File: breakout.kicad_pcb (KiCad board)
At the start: 2 copper layers, 24.1 x 52.9 mm, 5 parts

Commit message: Removed right edges fromt races.
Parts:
- added REF**: Vishay_PowerPAK_SC70-6L_Single, Package_TO_SOT_SMD:Vishay_PowerPAK_SC70-6L_Single, F.Cu at (124.7, 90.7)
- added REF**: Vishay_PowerPAK_SC70-6L_Dual, Package_TO_SOT_SMD:Vishay_PowerPAK_SC70-6L_Dual, F.Cu at (119.4, 104.4)
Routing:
- net (no net): track 946.0 -> 938.4 mm

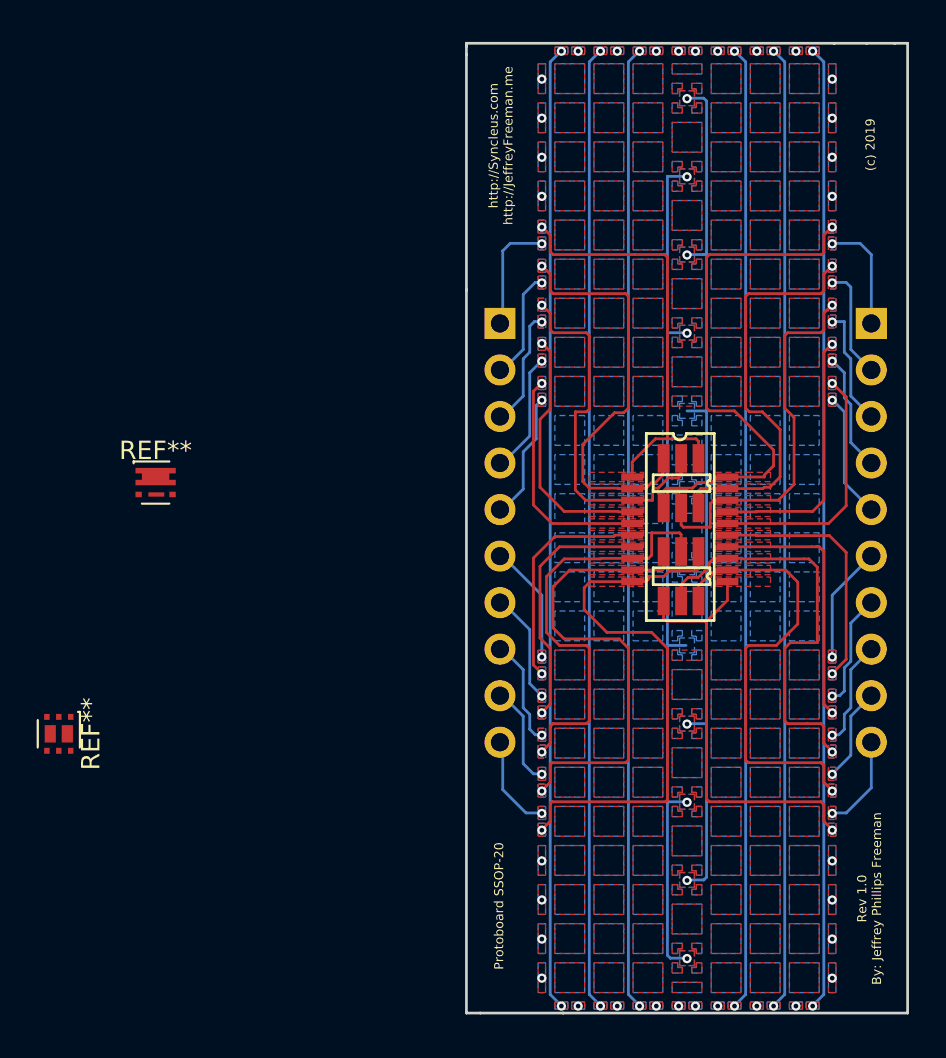
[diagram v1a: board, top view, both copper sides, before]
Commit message: Added labels for pin numbers and a few otehr graphics ont he silk screen.
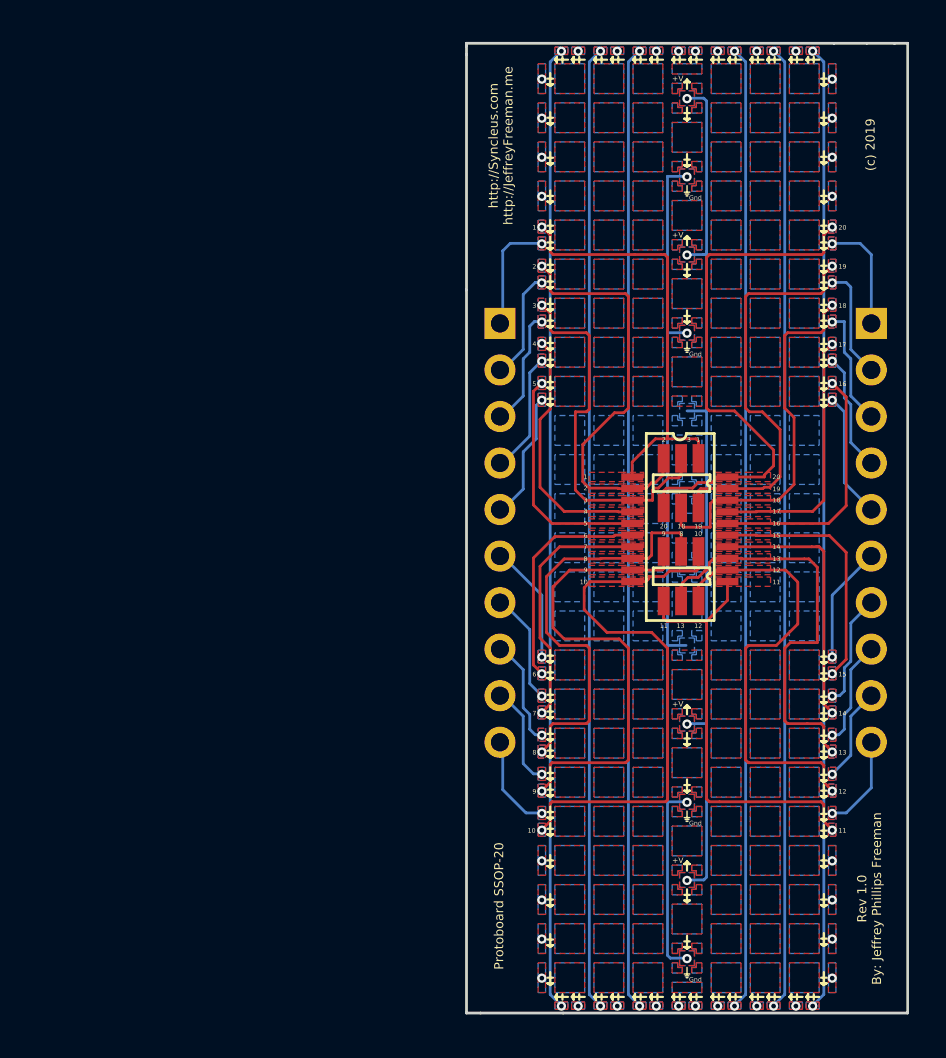
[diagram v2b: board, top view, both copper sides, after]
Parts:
- removed REF**: Vishay_PowerPAK_SC70-6L_Single, Package_TO_SOT_SMD:Vishay_PowerPAK_SC70-6L_Single
- removed REF**: Vishay_PowerPAK_SC70-6L_Dual, Package_TO_SOT_SMD:Vishay_PowerPAK_SC70-6L_Dual
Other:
- board text added: "+V"
- board text added: "1"
- board text added: "10"
- board text added: "11"
- board text added: "12"
- board text added: "13"
- board text added: "14"
- board text added: "15"
- board text added: "16"
- board text added: "17"
- board text added: "18"
- board text added: "19"
- board text added: "2"
- board text added: "20"
- board text added: "3"
- board text added: "4"
- board text added: "5"
- board text added: "6"
- board text added: "7"
- board text added: "8"
- board text added: "9"
- board text added: "Gnd"

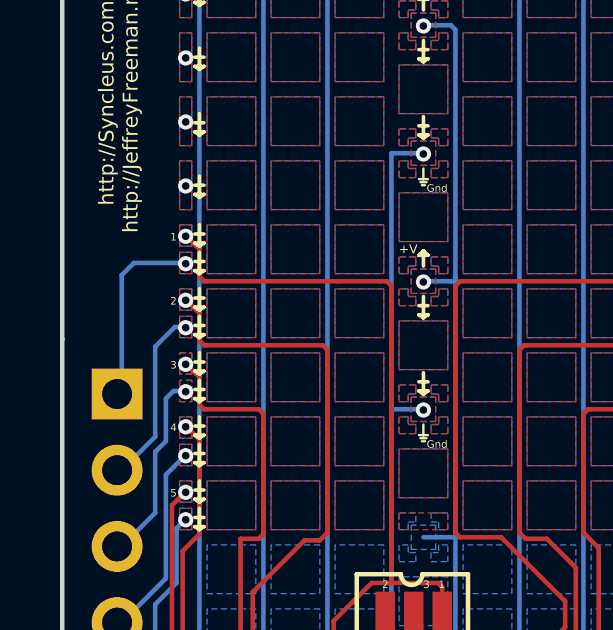
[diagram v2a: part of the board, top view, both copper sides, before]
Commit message: Changed fotn size a bit.
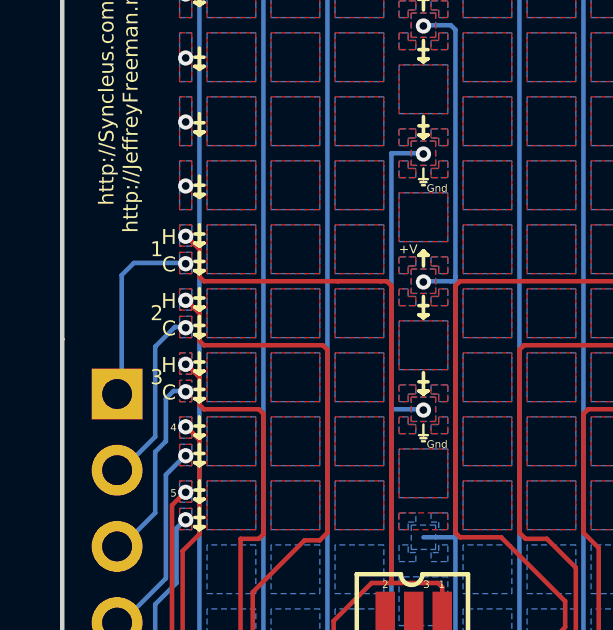
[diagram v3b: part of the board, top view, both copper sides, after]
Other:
- board text added: "C"
- board text added: "H"
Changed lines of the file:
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@@
   (general
     (thickness 1.6)
-    (drawings 1141)
+    (drawings 1147)
     (tracks 527)
     (zones 0)
@@
       (rotate (xyz 0 0 0))
     )
+  )
+  (gr_text 3 (at 144.8308 81.4832) (layer F.SilkS)
+    (effects (font (size 0.5 0.5) (thickness 0.0625)))
+  )
+  (gr_text H (at 145.2372 81.0768) (layer F.SilkS)
+    (effects (font (size 0.5 0.5) (thickness 0.0625)))
+  )
+  (gr_text C (at 145.2372 81.9912) (layer F.SilkS)
+    (effects (font (size 0.5 0.5) (thickness 0.0625)))
+  )
+  (gr_text 2 (at 144.8308 79.3496) (layer F.SilkS)
+    (effects (font (size 0.5 0.5) (thickness 0.0625)))
+  )
+  (gr_text H (at 145.2372 78.9432) (layer F.SilkS)
+    (effects (font (size 0.5 0.5) (thickness 0.0625)))
+  )
+  (gr_text C (at 145.2372 79.8576) (layer F.SilkS)
+    (effects (font (size 0.5 0.5) (thickness 0.0625)))
+  )
+  (gr_text C (at 145.2372 77.724) (layer F.SilkS)
+    (effects (font (size 0.5 0.5) (thickness 0.0625)))
+  )
+  (gr_text H (at 145.2372 76.8096) (layer F.SilkS)
+    (effects (font (size 0.5 0.5) (thickness 0.0625)))
   )
   (gr_line (start 153.7208 117.5512) (end 153.5684 117.5512) (layer F.SilkS) (width 0.08))
@@
     (effects (font (size 0.25 0.25) (thickness 0.0625)))
   )
-  (gr_text 3 (at 145.3896 81.0768) (layer F.SilkS)
-    (effects (font (size 0.25 0.25) (thickness 0.0625)))
-  )
-  (gr_text 2 (at 145.3896 78.9432) (layer F.SilkS)
-    (effects (font (size 0.25 0.25) (thickness 0.0625)))
-  )
-  (gr_text 1 (at 145.3896 76.8096) (layer F.SilkS)
-    (effects (font (size 0.25 0.25) (thickness 0.0625)))
+  (gr_text 1 (at 144.8308 77.216) (layer F.SilkS)
+    (effects (font (size 0.5 0.5) (thickness 0.0625)))
   )
   (gr_line (start 161.1884 110.1344) (end 161.036 110.0328) (layer F.SilkS) (width 0.12))
